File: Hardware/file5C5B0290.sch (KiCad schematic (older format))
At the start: 30 parts, among them J15 Eurorack Connector, J19 Power_Connector, U10 LM1117-3.3, U11 LM1117-5.0, U12 L7809, U9 LM1117-3.3

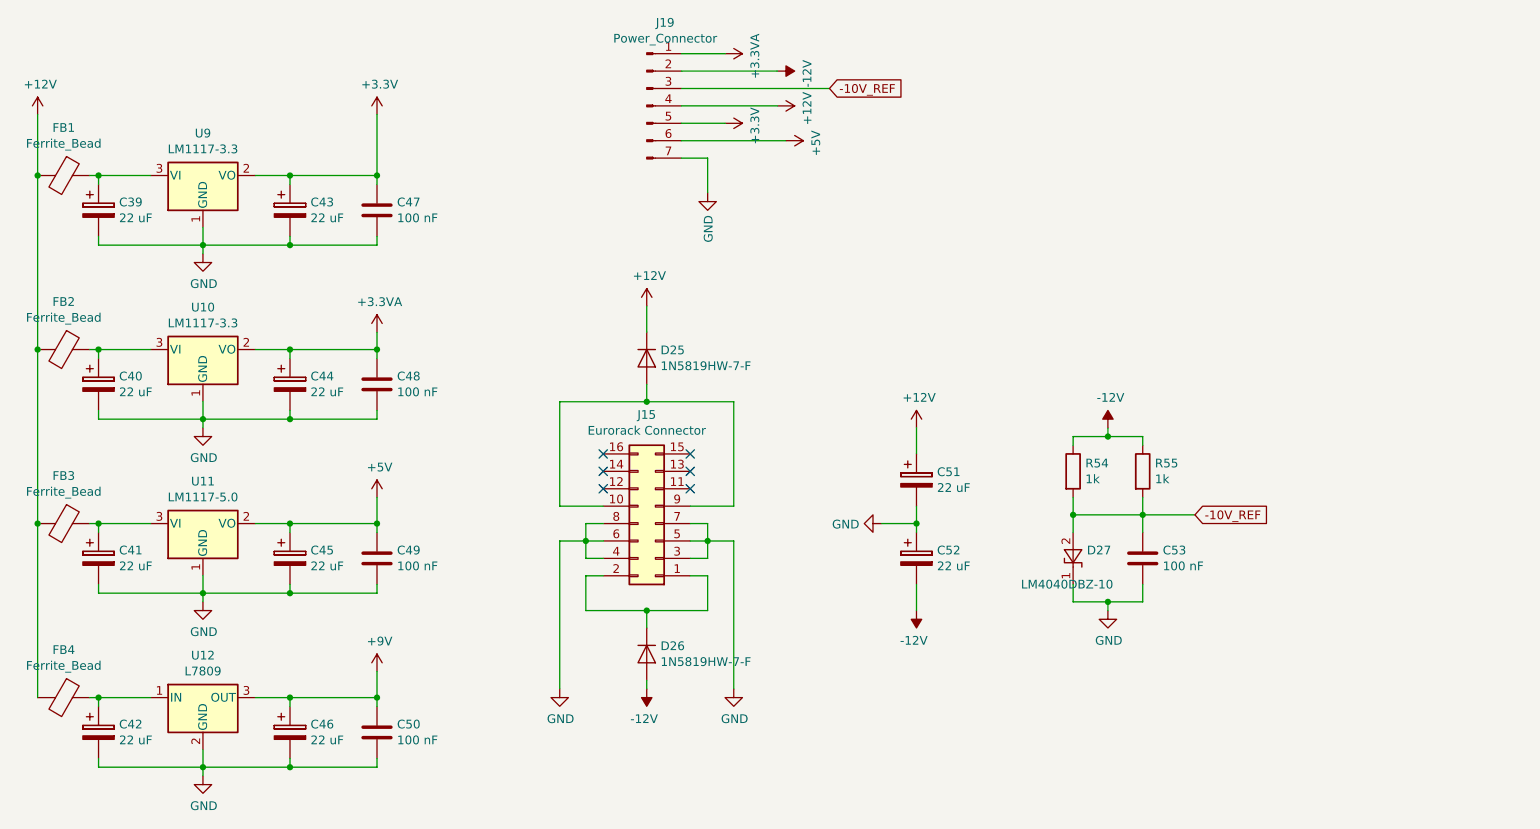
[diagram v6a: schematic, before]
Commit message: STM32CubeMX Blinky
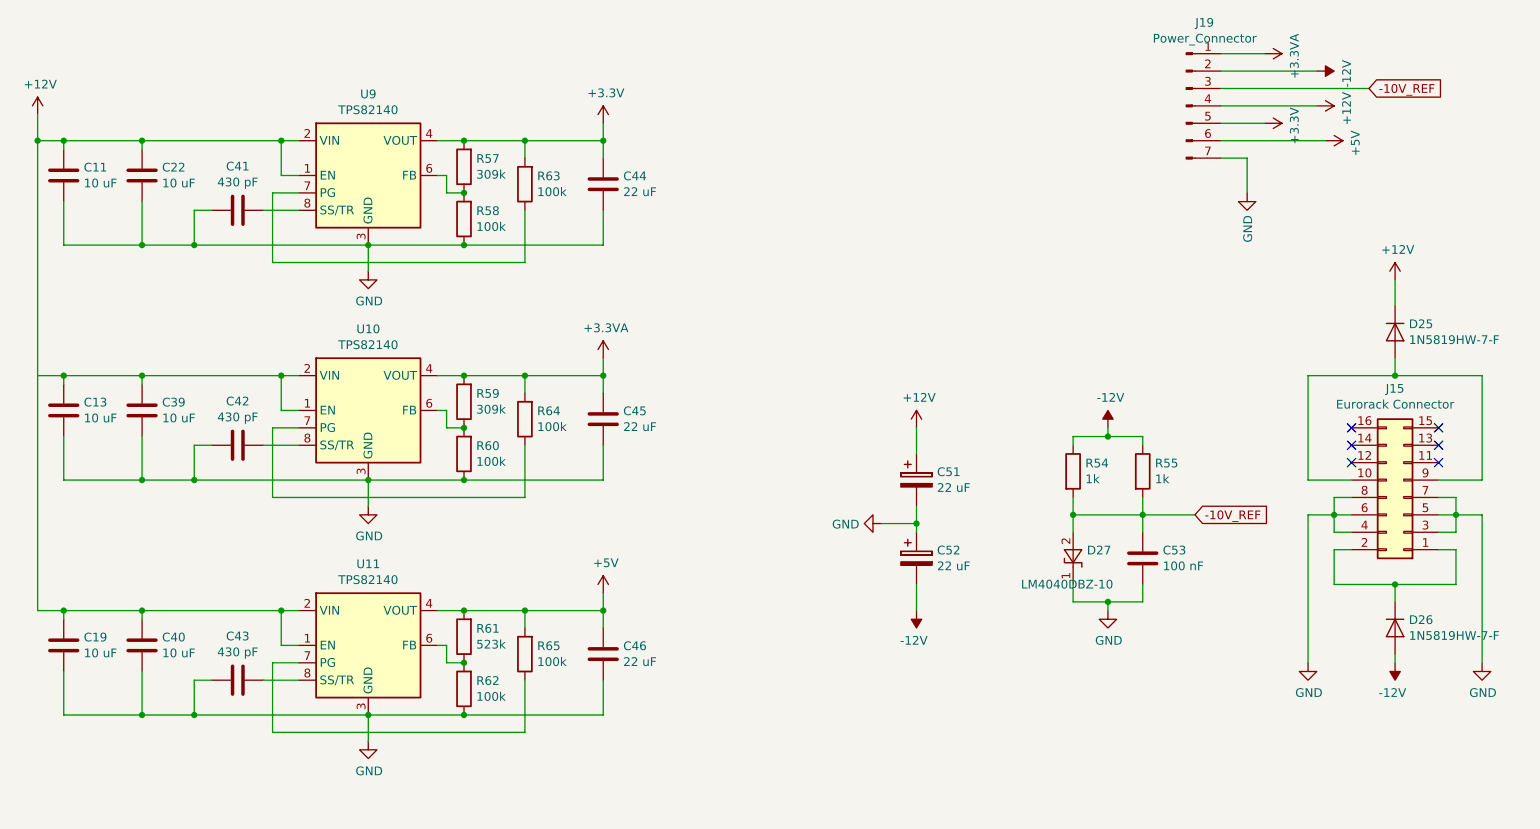
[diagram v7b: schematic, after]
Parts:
- removed C39, C40, C41, C42, C43, C44, C45, C46: 22 uF, Capacitor_SMD:CP_Elec_4x5.3, symbol Device:CP
- removed C47, C48, C49, C50: 100 nF, Capacitor_SMD:C_0603_1608Metric, symbol Device:C
- removed FB1, FB2, FB3, FB4: Ferrite_Bead, Inductor_SMD:L_0603_1608Metric, symbol Device:Ferrite_Bead
- removed U10, U9: LM1117-3.3, Package_TO_SOT_SMD:SOT-223-3_TabPin2, symbol Regulator_Linear:LM1117-3.3
- removed U11: LM1117-5.0, Package_TO_SOT_SMD:SOT-223-3_TabPin2, symbol Regulator_Linear:LM1117-5.0
- removed U12: L7809, Package_TO_SOT_SMD:TO-252-3_TabPin2, symbol Regulator_Linear:L7809
- added C11, C13, C19, C22, C39, C40: 10 uF, Capacitor_SMD:C_0603_1608Metric, symbol Device:C
- added C41, C42, C43: 430 pF, Capacitor_SMD:C_0603_1608Metric, symbol Device:C
- added C44, C45, C46: 22 uF, Capacitor_SMD:C_0603_1608Metric, symbol Device:C
- added R57, R59: 309k, Resistor_SMD:R_0603_1608Metric, symbol Device:R
- added R58, R60, R62, R63, R64, R65: 100k, Resistor_SMD:R_0603_1608Metric, symbol Device:R
- added R61: 523k, Resistor_SMD:R_0603_1608Metric, symbol Device:R
- added U10, U11, U9: TPS82140, TPS82140SILR:PSON65P280X300X153-9N, symbol Regulator_Switching:TPS82140
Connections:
- net +12V: now also C11.1, C13.1, C19.1, C22.1, C39.1, C40.1, U10.1 (EN), U10.2 (VIN), U11.1 (EN), U11.2 (VIN), U9.1 (EN), U9.2 (VIN)
- net +3.3VA: now also C45.1, R59.2, R64.2, U10.4 (VOUT), U10.5 (VOUT)
- net +3V3: now also C44.1, R57.2, R63.2, U9.4 (VOUT), U9.5 (VOUT)
- net +5V: now also C46.1, R61.2, R65.2, U11.4 (VOUT), U11.5 (VOUT)
- net GND: now also C11.2, C13.2, C19.2, C22.2, C39.2, C40.2, C41.1, C42.1, C43.1, C44.2, C45.2, C46.2, R58.1, R60.1, R62.1, U10.3 (GND), U10.9 (GND), U11.3 (GND), U11.9 (GND), U9.3 (GND), U9.9 (GND)
- new net: R57.1, R58.2, U9.6 (FB)
- new net: R63.1, U9.7 (PG)
- new net: C41.2, U9.8 (SS/TR)
- new net: R59.1, R60.2, U10.6 (FB)
- new net: R64.1, U10.7 (PG)
- new net: C42.2, U10.8 (SS/TR)
- new net: R61.1, R62.2, U11.6 (FB)
- new net: R65.1, U11.7 (PG)
- new net: C43.2, U11.8 (SS/TR)
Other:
- moved on the sheet: D25, D26, J15, J19
